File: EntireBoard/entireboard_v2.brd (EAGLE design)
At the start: 60 x 60 mm, 47 parts, among them J1 FTSH-105-01-XXX-DV-K, P1 0532610271, U1 YKA, U2 RHD2216_QFN

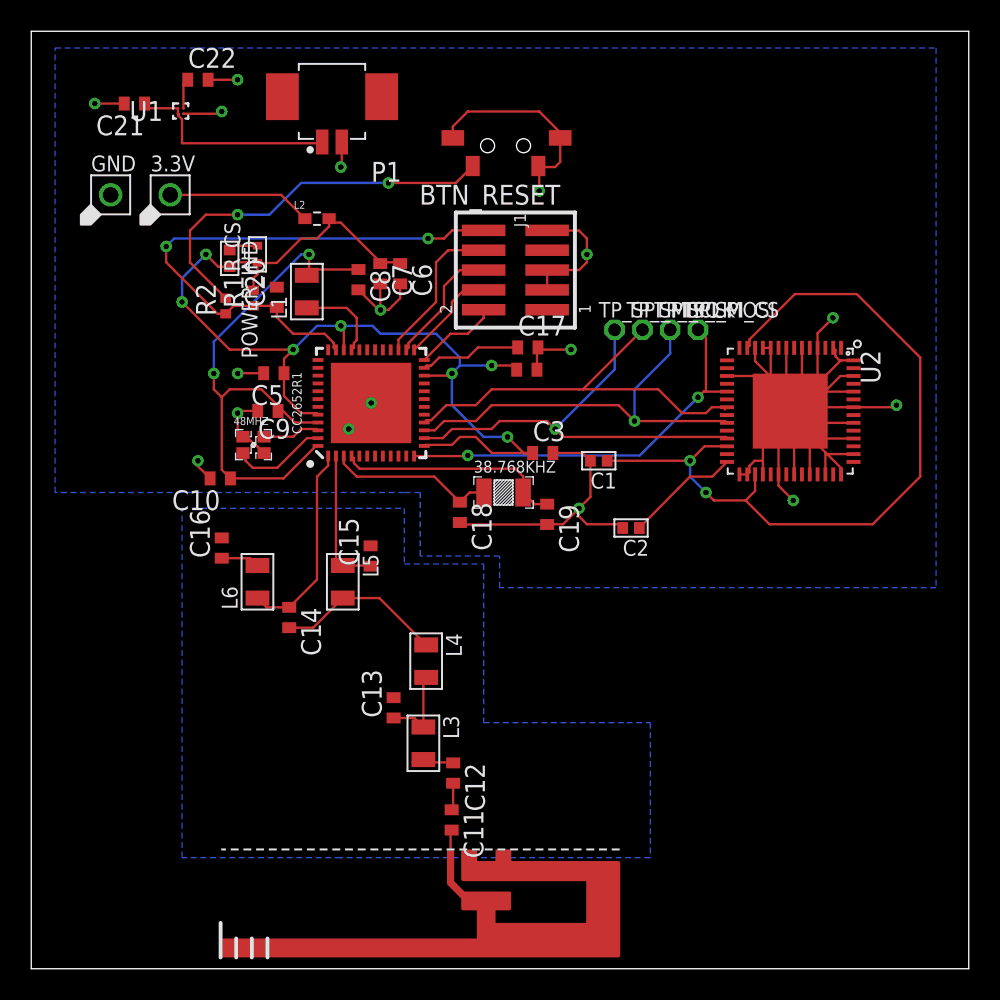
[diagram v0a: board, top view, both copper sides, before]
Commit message: 2 layer 6x6 cm board
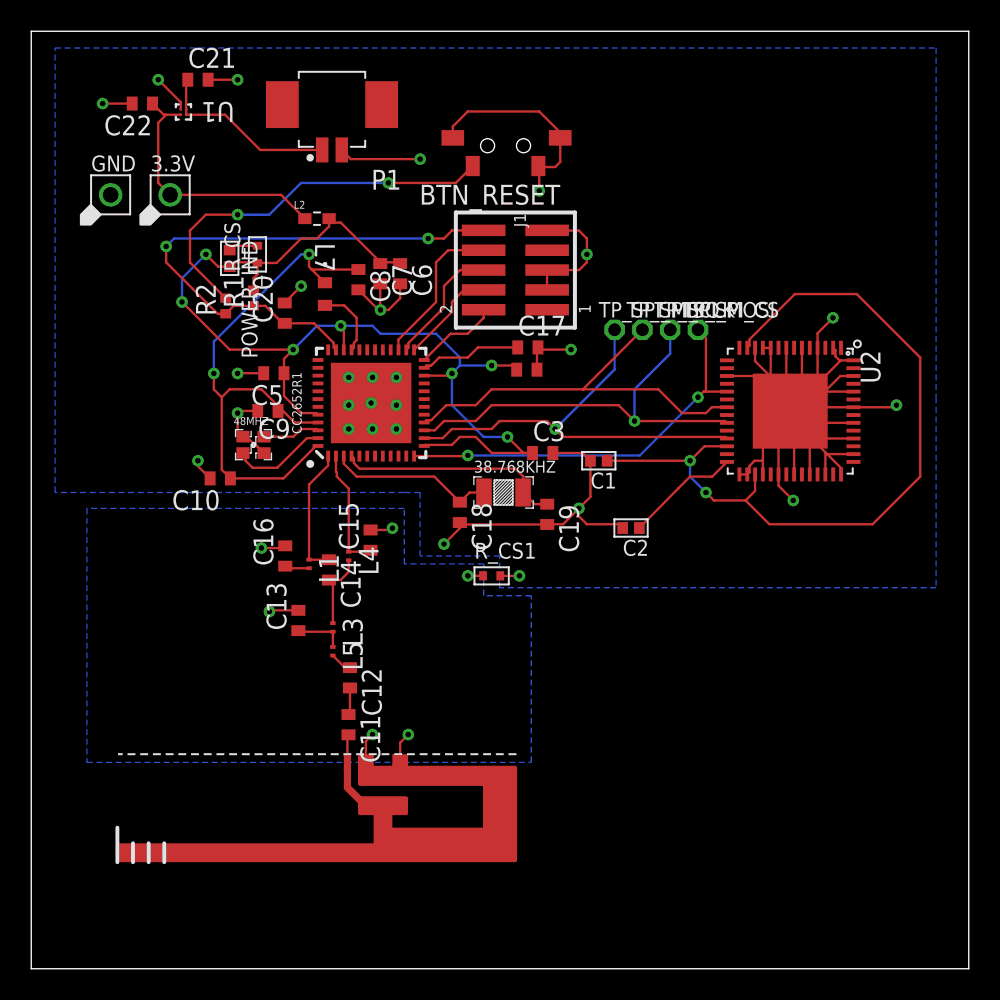
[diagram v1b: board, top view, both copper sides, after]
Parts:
- removed L6: 2.4nH, AxonMobile:RHD2000_EVAL_BOARD_0805
- added L7: AIML-0603-6R8K-T, inductor_0603:AIML-0603
- added R_CS1: 0.01ohm, MF_Passives:R0402
- L1: value 6.8uH -> 2.4nH; device AxonMobile:RHD2000_EVAL_BOARD_0805 -> rcl-2:L0201
- L3: device AxonMobile:RHD2000_EVAL_BOARD_0805 -> rcl-2:L0201
- L4: value 2nH -> 2.4nH; device AxonMobile:RHD2000_EVAL_BOARD_0805 -> rcl-2:L0201
- L5: value 2.4nH -> 2nH; device AxonMobile:RHD2000_EVAL_BOARD_0805 -> rcl-2:L0201
- moved L1 17.4 mm to (17.8, 25.9), turned to 270 degrees
- moved L3 9.41 mm to (19.3, 21.8)
- moved C11 8.99 mm to (20.3, 15.6)
- moved U$2 8.99 mm to (22.5, 10.4)
- moved C12 8.99 mm to (20.4, 18.6)
- moved L4 8.36 mm to (20.3, 26.4)
- moved C13 8.27 mm to (17.1, 22.3)
- moved L5 4.49 mm to (19.3, 20.3)
- moved C21 4.34 mm to (10.7, 56.9), turned to 0 degrees
- moved C16 4.10 mm to (16.3, 26.4)
- moved C14 3.97 mm to (19.1, 25.5)
- moved C22 3.87 mm to (7.11, 55.4), turned to 180 degrees
- moved C20 1.14 mm to (16.2, 42.0)
- moved C15 1.02 mm to (21.7, 27.4)
- moved P1 0.51 mm to (19.2, 52.4)
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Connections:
- net DCDC_SW: now also L7.2; no longer L1.1
- net GND: now also R_CS1.P$1, R_CS1.P$2
- net N$12: now also L1.2; no longer L6.2
- net N$7: now also L5.2; no longer L3.2
- net N$8: now also L3.2, L5.1; no longer L3.1, L4.2
- net N$9: now also L3.1, L4.2; no longer L4.1, L5.2
- net RF_N: now also L4.1; no longer L5.1
- net RF_P: now also L1.1; no longer L6.1
- net VDDR: now also L7.1; no longer L1.2
- net VDDS: no longer C22.1, U1.A2
- net WMCU_VDD: now also C22.1, U1.A2
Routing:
- net GND: track 136.8 -> 154.4 mm, vias 16 -> 25
- net WMCU_VDD: track 9.25 -> 17.0 mm
- net N$9: track 10.8 -> 5.09 mm
- net RF_P: track 13.0 -> 8.40 mm
- net N$8: track 5.39 -> 3.21 mm
- net VDDS: track 74.0 -> 72.0 mm
- net N$7: track 2.89 -> 1.41 mm
- net N$14: track 13.6 -> 12.4 mm
- net DCDC_SW: track 5.64 -> 4.55 mm
- net RF_N: track 8.98 -> 7.89 mm
- net N$12: track 2.48 -> 1.58 mm

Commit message: added test LEDs, still 2 layers
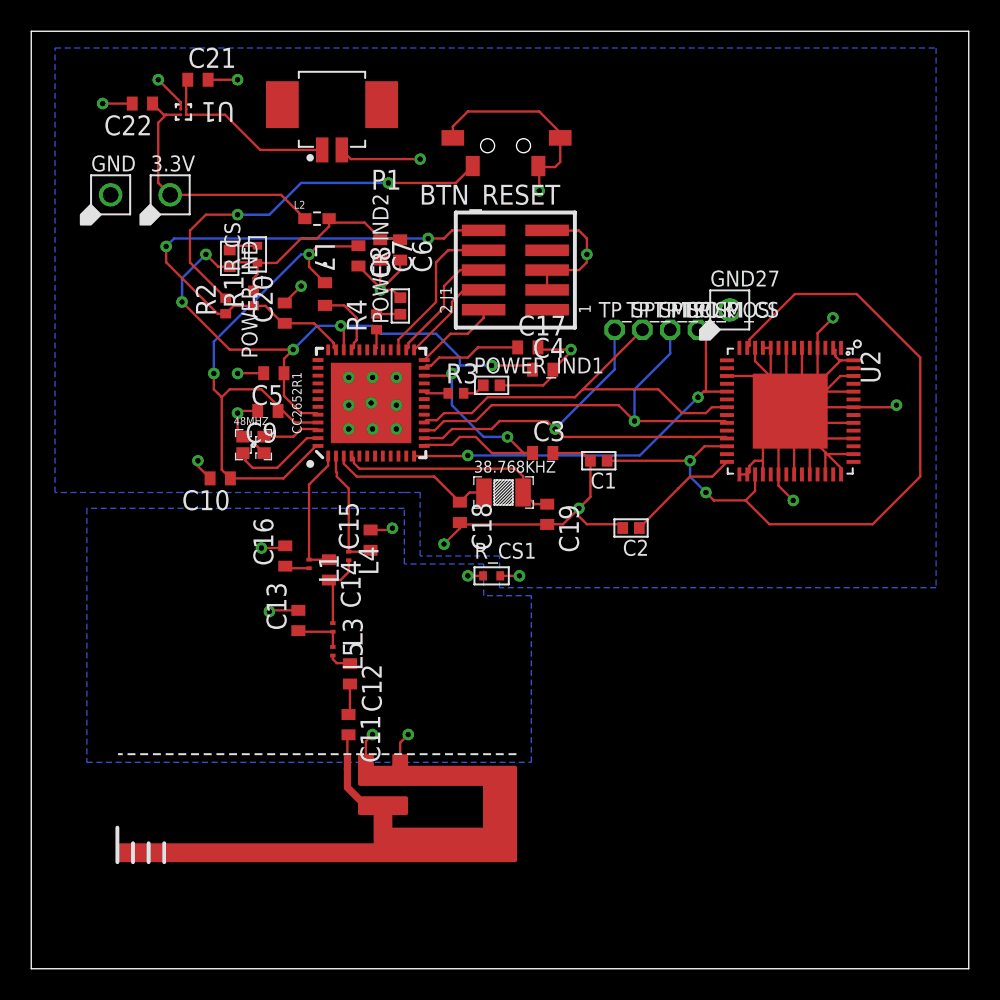
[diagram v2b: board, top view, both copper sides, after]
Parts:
- added GND27: MF-CON-2.54mm-01x01, AxonMobile:PTH_2.54MM_01X01
- added POWER_IND1, POWER_IND2: LED-SMD, AxonMobile:RHD2000_EVAL_BOARD_0402
- added R3, R4: (no value), AxonMobile:R0402
- moved C6 1.52 mm to (23.6, 46.0)
- moved C7 1.52 mm to (22.3, 46.0)
- moved C8 1.52 mm to (20.9, 45.6)
- moved C4 1.02 mm to (32.7, 38.3)
- moved C12 0.25 mm to (20.4, 18.9)
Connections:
- new net N$23: CC2652R1.20, R3.1
- new net N$24: POWER_IND1.1, R3.2
- new net N$25: CC2652R1.30, R4.1
- new net N$26: POWER_IND2.1, R4.2
- net GND: now also GND27.P$1, POWER_IND1.2, POWER_IND2.2
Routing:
- net GND: track 154.4 -> 160.7 mm
- net N$23: track 0.00 -> 1.58 mm
- net N$26: track 0.00 -> 1.53 mm
- net N$24: track 0.00 -> 1.46 mm
- net N$25: track 0.00 -> 1.33 mm
